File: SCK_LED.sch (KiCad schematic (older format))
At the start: 4 parts, among them U1 LMV358, U4 LMV358

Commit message: Set component footprints, added datasheets, fixed the last DRC error and a couple component values
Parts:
- D3: footprint (none) -> LED_SMD:LED_0603_1608Metric
- R4: footprint (none) -> Resistor_SMD:R_0603_1608Metric
- U1, U4: footprint (none) -> Package_SO:MSOP-8_3x3mm_P0.65mm
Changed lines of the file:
@@
 F 0 "U1" H 5800 4000 50  0000 C CNN
 F 1 "LMV358" H 5850 3900 50  0000 C CNN
-F 2 "" H 5750 3700 50  0001 C CNN
-F 3 "http://www.ti.com/lit/ds/symlink/lmv324.pdf" H 5750 3700 50  0001 C CNN
+F 2 "Package_SO:MSOP-8_3x3mm_P0.65mm" H 5750 3700 50  0001 C CNN
+F 3 "http://www.farnell.com/datasheets/2140563.pdf" H 5750 3700 50  0001 C CNN
 	2    5750 3700
 	1    0    0    -1
@@
 F 0 "U4" H 5708 3700 50  0001 L CNN
 F 1 "LMV358" H 5708 3655 50  0001 L CNN
-F 2 "" H 5750 3700 50  0001 C CNN
-F 3 "http://www.ti.com/lit/ds/symlink/lmv324.pdf" H 5750 3700 50  0001 C CNN
+F 2 "Package_SO:MSOP-8_3x3mm_P0.65mm" H 5750 3700 50  0001 C CNN
+F 3 "http://www.farnell.com/datasheets/2140563.pdf" H 5750 3700 50  0001 C CNN
 	3    5750 3700
 	1    0    0    -1
@@
 F 0 "R4" H 6370 3946 50  0000 L CNN
 F 1 "510R" H 6370 3855 50  0000 L CNN
-F 2 "" V 6230 3900 50  0001 C CNN
-F 3 "~" H 6300 3900 50  0001 C CNN
+F 2 "Resistor_SMD:R_0603_1608Metric" V 6230 3900 50  0001 C CNN
+F 3 "http://www.farnell.com/datasheets/2310790.pdf" H 6300 3900 50  0001 C CNN
 	1    6300 3900
 	1    0    0    -1
@@
 F 0 "D3" V 6339 4133 50  0000 R CNN
 F 1 "SCK_LED" V 6248 4133 50  0000 R CNN
-F 2 "" H 6300 4250 50  0001 C CNN
-F 3 "~" H 6300 4250 50  0001 C CNN
+F 2 "LED_SMD:LED_0603_1608Metric" H 6300 4250 50  0001 C CNN
+F 3 "http://www.farnell.com/datasheets/1681524.pdf" H 6300 4250 50  0001 C CNN
 	1    6300 4250
 	0    -1   -1   0
@@
 ICSP_SCK
 $Comp
-L power:PWR_FLAG #FLG0101
+L power:PWR_FLAG #FLG04
 U 1 1 5ED9930A
 P 5650 3350
-F 0 "#FLG0101" H 5650 3425 50  0001 C CNN
+F 0 "#FLG04" H 5650 3425 50  0001 C CNN
 F 1 "PWR_FLAG" V 5650 3477 50  0000 L CNN
 F 2 "" H 5650 3350 50  0001 C CNN

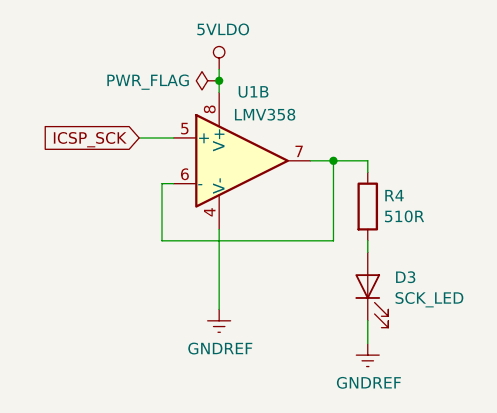
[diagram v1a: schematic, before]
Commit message: Updated the schematic, added missing footprints, started PCB design
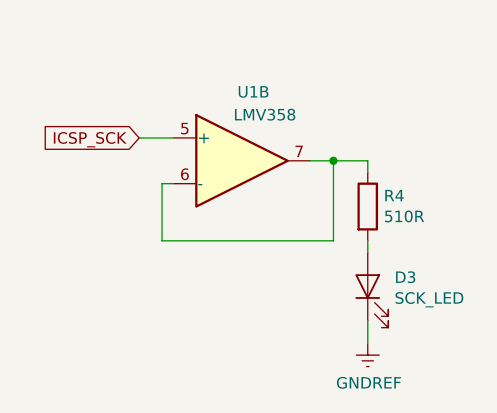
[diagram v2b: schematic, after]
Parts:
- removed U4: LMV358, Package_SO:MSOP-8_3x3mm_P0.65mm, symbol Amplifier_Operational:LMV358
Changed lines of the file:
@@
 Wire Wire Line
 	5300 3600 5450 3600
-$Comp
-L power_symbols:5VLDO #PWR013
-U 1 1 5EC7A6A5
-P 5650 3300
-F 0 "#PWR013" H 5650 3150 50  0001 C CNN
-F 1 "5VLDO" H 5667 3473 50  0000 C CNN
-F 2 "" H 5650 3300 50  0001 C CNN
-F 3 "" H 5650 3300 50  0001 C CNN
-	1    5650 3300
-	1    0    0    -1
-$EndComp
-$Comp
-L Amplifier_Operational:LMV358 U4
-U 3 1 5EC7A6AB
-P 5750 3700
-F 0 "U4" H 5708 3700 50  0001 L CNN
-F 1 "LMV358" H 5708 3655 50  0001 L CNN
-F 2 "Package_SO:MSOP-8_3x3mm_P0.65mm" H 5750 3700 50  0001 C CNN
-F 3 "http://www.farnell.com/datasheets/2140563.pdf" H 5750 3700 50  0001 C CNN
-	3    5750 3700
-	1    0    0    -1
-$EndComp
-Wire Wire Line
-	5650 3300 5650 3350
-$Comp
-L power:GNDREF #PWR014
-U 1 1 5EC7A6B2
-P 5650 4350
-F 0 "#PWR014" H 5650 4100 50  0001 C CNN
-F 1 "GNDREF" H 5655 4177 50  0000 C CNN
-F 2 "" H 5650 4350 50  0001 C CNN
-F 3 "" H 5650 4350 50  0001 C CNN
-	1    5650 4350
-	1    0    0    -1
-$EndComp
-Wire Wire Line
-	5650 4350 5650 4000
 Wire Wire Line
 	5450 3800 5400 3800
@@
 Text GLabel 5300 3600 0    50   Input ~ 0
 ICSP_SCK
-$Comp
-L power:PWR_FLAG #FLG04
-U 1 1 5ED9930A
-P 5650 3350
-F 0 "#FLG04" H 5650 3425 50  0001 C CNN
-F 1 "PWR_FLAG" V 5650 3477 50  0000 L CNN
-F 2 "" H 5650 3350 50  0001 C CNN
-F 3 "~" H 5650 3350 50  0001 C CNN
-	1    5650 3350
-	0    -1   -1   0
-$EndComp
-Connection ~ 5650 3350
-Wire Wire Line
-	5650 3350 5650 3400
 $EndSCHEMATC
